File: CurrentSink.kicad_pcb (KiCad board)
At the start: 2 copper layers, 22 parts, among them J101 Test-Source, J102 Power-Jumper, J103 Power-Connector, Q301 STP55NF06L, U201 MCP6002, U401 TPS7A2401

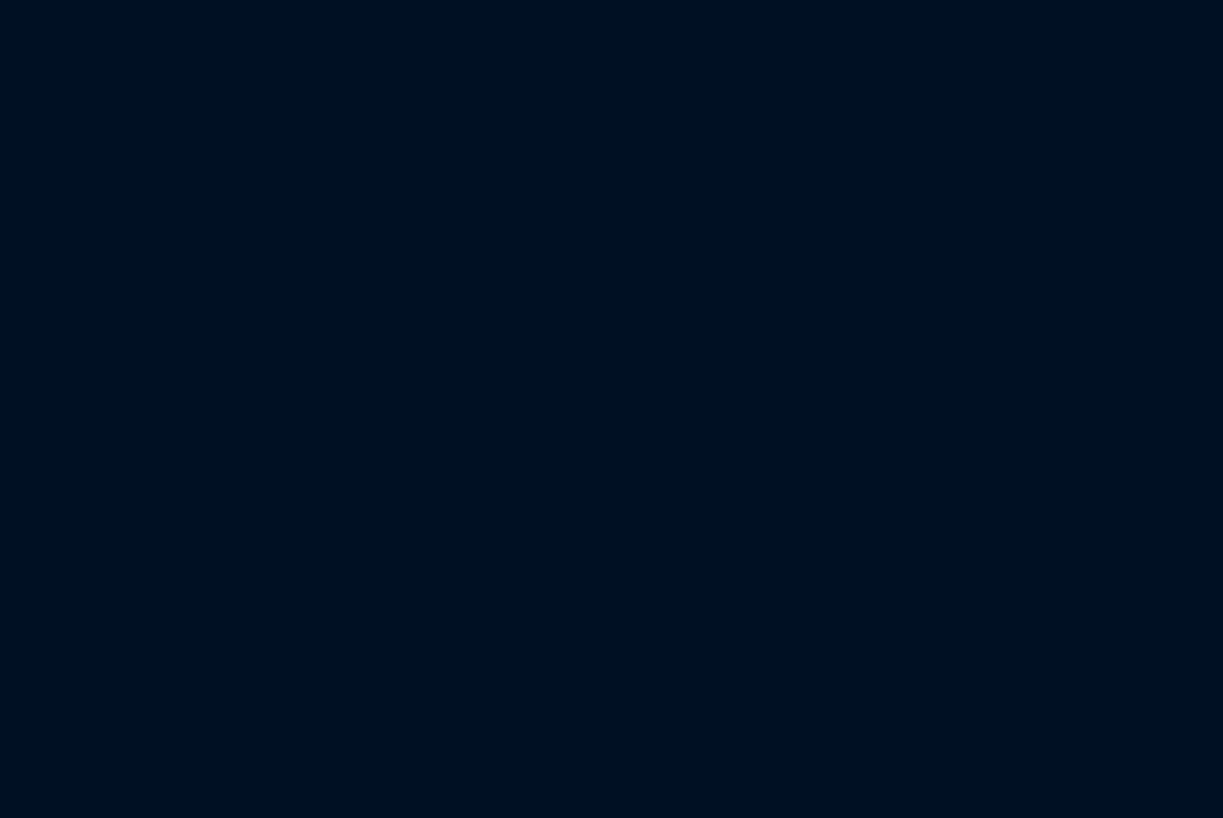
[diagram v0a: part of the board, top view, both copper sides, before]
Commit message: Added heatsink to schematic and PCB
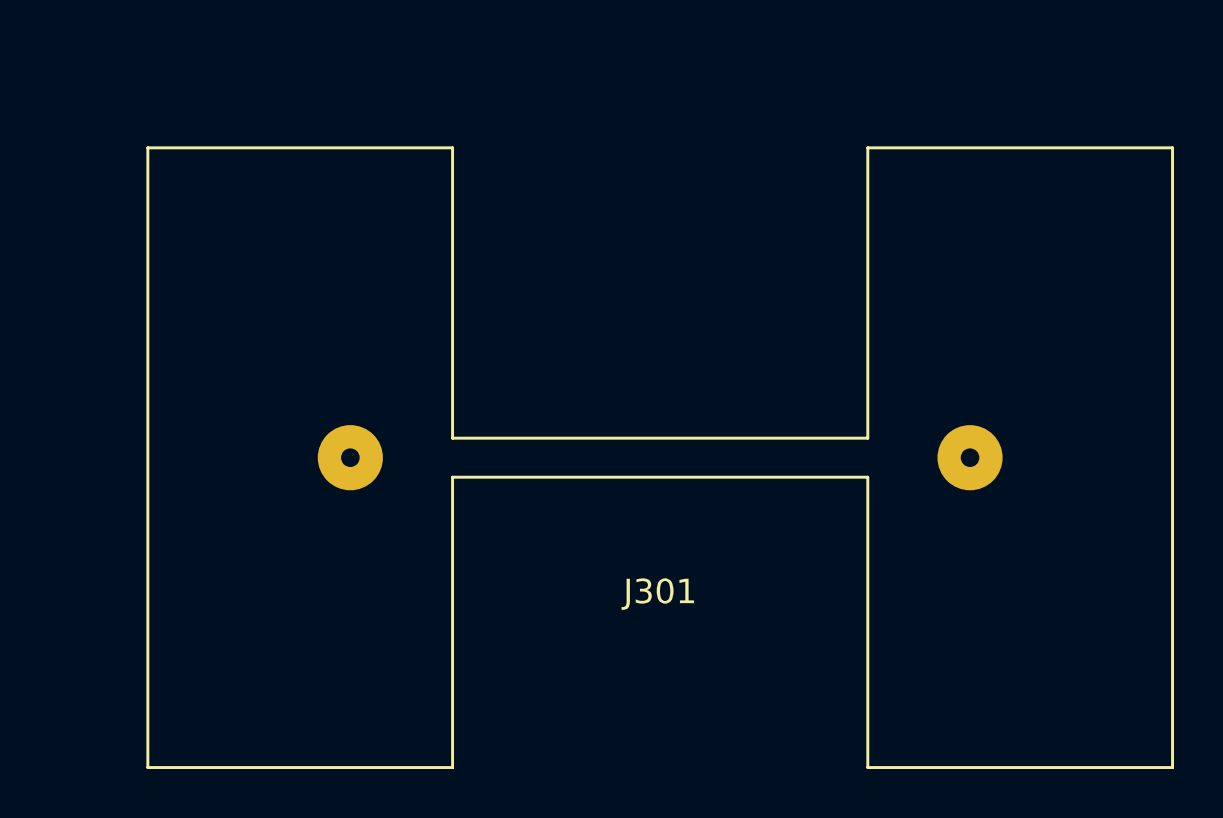
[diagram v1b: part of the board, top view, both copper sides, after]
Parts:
- added J301: Heatsink, f:Heatsink, F.Cu at (160.6, 81.0)

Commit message: Initial PCB component Placement
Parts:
- J101: value Test-Source -> Test; footprint Connector_PinHeader_1.27mm:PinHeader_1x02_P1.27mm_Vertical -> Connector_PinHeader_1.27mm:PinHeader_1x02_P1.27mm_Horizontal
- J103: value Power-Connector -> Ext. Pwr; footprint Connector_BarrelJack:BarrelJack_CUI_PJ-036AH-SMT_Horizontal -> TerminalBlock_Phoenix:TerminalBlock_Phoenix_PT-1,5-2-5.0-H_1x02_P5.00mm_Horizontal
- moved RV301 94.0 mm to (139.1, 146.4), turned to 270 degrees
- moved J103 85.2 mm to (118.0, 142.0)
- moved R301 84.9 mm to (142.9, 142.3), turned to 270 degrees
- moved J101 84.1 mm to (113.3, 141.5), turned to 270 degrees
- moved J102 75.8 mm to (107.2, 127.2)
- moved D201 74.9 mm to (140.6, 135.1)
- moved R302 74.4 mm to (143.2, 131.8), turned to 180 degrees
- moved RV201 73.7 mm to (129.6, 146.4), turned to 270 degrees
- moved R201 69.5 mm to (133.4, 142.3), turned to 270 degrees
- moved U201 65.0 mm to (137.2, 129.9), turned to 180 degrees
- moved R303 64.9 mm to (128.3, 123.0), turned to 270 degrees
- moved Q301 64.0 mm to (122.5, 117.0)
- moved R402 58.4 mm to (117.7, 133.0), turned to 270 degrees
- moved C404 57.7 mm to (129.1, 132.3), turned to 270 degrees
- moved R403 53.9 mm to (111.5, 133.0), turned to 90 degrees
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
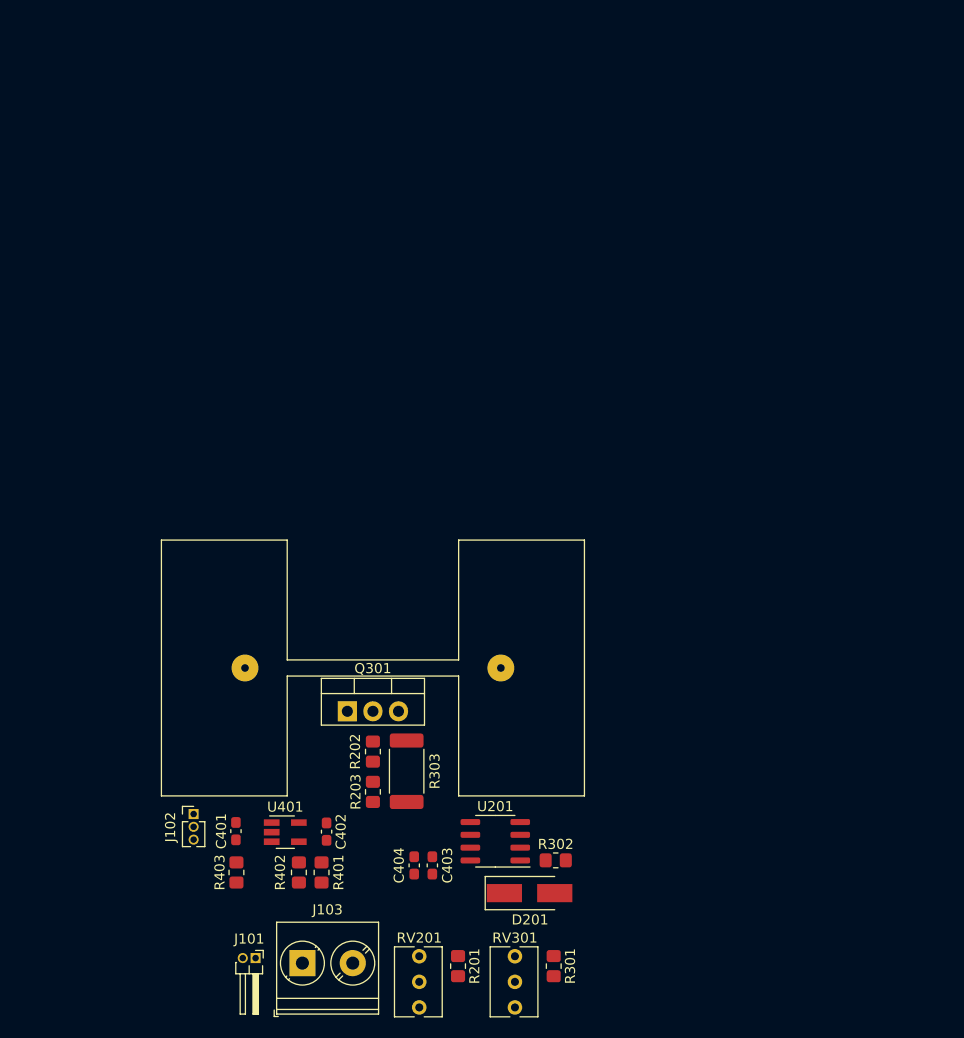
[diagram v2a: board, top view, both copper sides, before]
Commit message: PCB completed with Op-Amp mounted horizontally
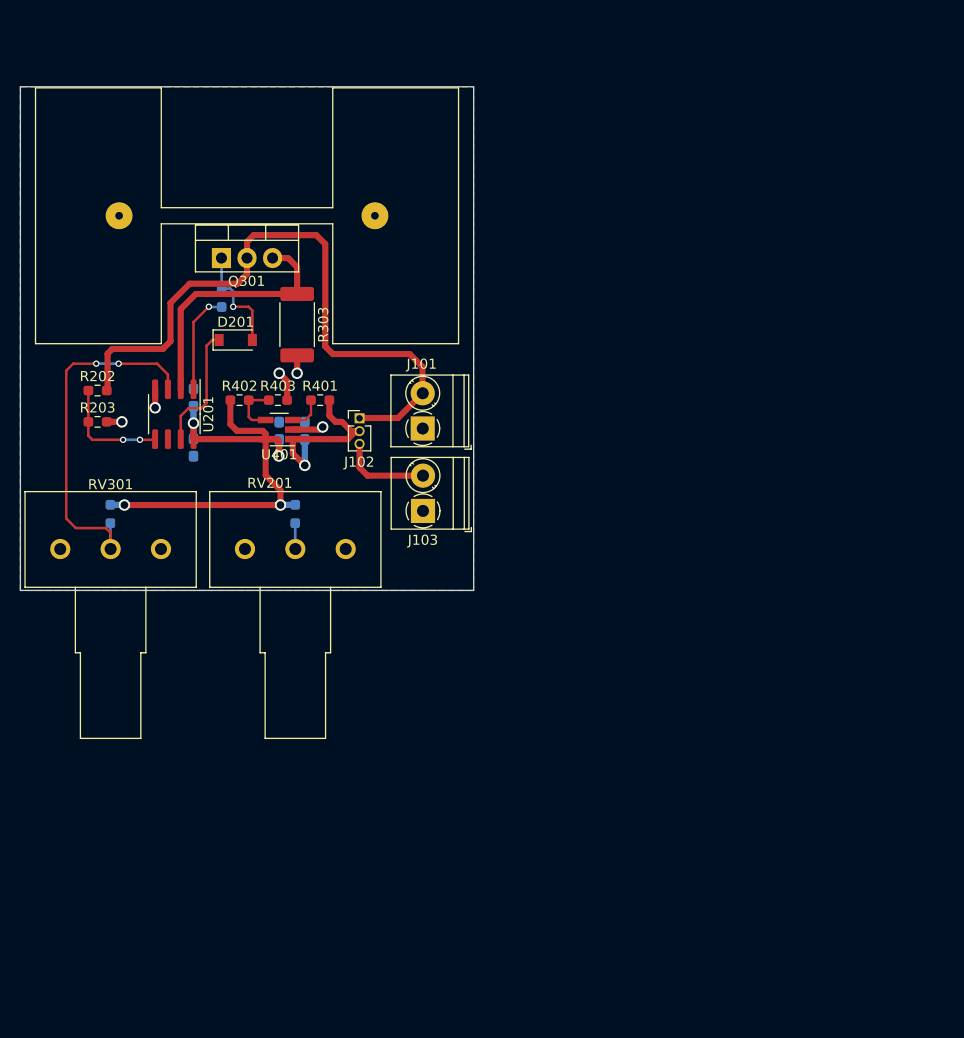
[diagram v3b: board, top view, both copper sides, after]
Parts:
- removed J301: Heatsink, f:Heatsink
- added H301: Heatsink, f:Heatsink, F.Cu at (112.5, 67.8)
- C401, C402, C403, C404: moved to B.Cu
- D201: value D -> 1N4148; footprint Diode_SMD:D_SMA_Handsoldering -> Diode_SMD:D_SOD-123
- J101: value Test -> Tst; footprint Connector_PinHeader_1.27mm:PinHeader_1x02_P1.27mm_Horizontal -> TerminalBlock_Phoenix:TerminalBlock_Phoenix_PT-1,5-2-3.5-H_1x02_P3.50mm_Horizontal
- J102: value Power-Jumper -> pwrJmp
- J103: value Ext. Pwr -> Pwr; footprint TerminalBlock_Phoenix:TerminalBlock_Phoenix_PT-1,5-2-5.0-H_1x02_P5.00mm_Horizontal -> TerminalBlock_Phoenix:TerminalBlock_Phoenix_PT-1,5-2-3.5-H_1x02_P3.50mm_Horizontal
- R201: value R -> 1K; footprint Resistor_SMD:R_0805_2012Metric_Pad1.20x1.40mm_HandSolder -> Resistor_SMD:R_0603_1608Metric_Pad0.98x0.95mm_HandSolder; moved to B.Cu
- R202, R203, R402: footprint Resistor_SMD:R_0805_2012Metric_Pad1.20x1.40mm_HandSolder -> Resistor_SMD:R_0603_1608Metric_Pad0.98x0.95mm_HandSolder
- R301: value R -> 6.2K; footprint Resistor_SMD:R_0805_2012Metric_Pad1.20x1.40mm_HandSolder -> Resistor_SMD:R_0603_1608Metric_Pad0.98x0.95mm_HandSolder; moved to B.Cu
- R302: footprint Resistor_SMD:R_0805_2012Metric_Pad1.20x1.40mm_HandSolder -> Resistor_SMD:R_0603_1608Metric_Pad0.98x0.95mm_HandSolder; moved to B.Cu
- R401: value 10K -> 0; footprint Resistor_SMD:R_0805_2012Metric_Pad1.20x1.40mm_HandSolder -> Resistor_SMD:R_0603_1608Metric_Pad0.98x0.95mm_HandSolder
- R403: value 0 -> 10K; footprint Resistor_SMD:R_0805_2012Metric_Pad1.20x1.40mm_HandSolder -> Resistor_SMD:R_0603_1608Metric_Pad0.98x0.95mm_HandSolder
- RV201, RV301: value R_POT -> 10K; footprint Potentiometer_THT:Potentiometer_Bourns_3266Y_Vertical -> f:POT_TTElect_P160KN
- moved R302 65.0 mm to (110.0, 75.9), turned to 270 degrees
- moved R301 62.9 mm to (98.9, 97.4)
- moved D201 62.2 mm to (111.4, 80.1)
- moved RV301 60.7 mm to (99.0, 100.9), turned to 0 degrees
- moved J101 55.1 mm to (129.9, 88.9), turned to 90 degrees
- moved U201 53.0 mm to (105.3, 87.5), turned to 270 degrees
- moved C403 47.8 mm to (107.2, 90.8)
- moved R201 47.7 mm to (117.3, 97.4)
- moved R402 47.3 mm to (111.8, 86.1), turned to 0 degrees
- moved RV201 47.1 mm to (117.3, 100.9), turned to 0 degrees
- moved R403 47.1 mm to (115.6, 86.1), turned to 0 degrees
- moved R401 46.9 mm to (119.8, 86.1), turned to 0 degrees
- moved Q301 46.7 mm to (110.0, 72.0)
- moved J103 46.5 mm to (130.0, 97.1), turned to 90 degrees
- moved R203 45.8 mm to (97.7, 88.3), turned to 0 degrees
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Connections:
- net /V-ctrl renamed /Vctrl
- net /V-pos-tst renamed /tstV+
- C401 pad 1: /V-pos-src -> /regIN
- C402 pad 1: /2.5V-reg -> /2.5V
- C403 pad 1: /2.5V-reg -> /2.5V
- C404 pad 1: /2.5V-reg -> /2.5V
- J102 pad 2: /V-pos-src -> /regIN
- J102 pad 3: /V-pos-src -> /pwrV+
- J103 pad 1: /V-pos-src -> GND
- J103 pad 2: GND -> /pwrV+
- R201 pad 1: Net-(R201-Pad1) -> /2.5V
- R201 pad 2: GND -> Net-(R201-Pad2)
- R301 pad 1: Net-(R301-Pad1) -> /2.5V
- R301 pad 2: GND -> Net-(R301-Pad2)
- R401 pad 1: /2.5V-reg -> /Power-Reg/regEN
- R401 pad 2: /Power-Reg/FB -> /regIN
- R402 pad 1: /Power-Reg/FB -> /2.5V
- R402 pad 2: GND -> /Power-Reg/regFB
- R403 pad 1: Net-(R403-Pad1) -> /Power-Reg/regFB
- R403 pad 2: /V-pos-src -> GND
- RV201 pad 1: Net-(RV201-Pad1) -> GND
- RV201 pad 2: /2.5V-reg -> Net-(R201-Pad2)
- RV201 pad 3: Net-(R201-Pad1) -> Net-(RV201-Pad3)
- RV301 pad 1: Net-(RV301-Pad1) -> GND
- RV301 pad 2: /2.5V-reg -> Net-(R301-Pad2)
- RV301 pad 3: Net-(R301-Pad1) -> Net-(RV301-Pad3)
- U201 pad 3: Net-(R301-Pad1) -> Net-(R301-Pad2)
- U201 pad 5: Net-(R201-Pad1) -> Net-(R202-Pad2)
- U201 pad 6: Net-(R202-Pad2) -> Net-(R201-Pad2)
- U201 pad 8: /2.5V-reg -> /2.5V
- U401 pad 1: /V-pos-src -> /regIN
- U401 pad 3: Net-(R403-Pad1) -> /Power-Reg/regEN
- U401 pad 4: /Power-Reg/FB -> /Power-Reg/regFB
- U401 pad 5: /2.5V-reg -> /2.5V
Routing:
- net /tstV+: track 0.00 -> 65.3 mm
- net /2.5V: track 0.00 -> 48.8 mm, vias 0 -> 4
- net Net-(R301-Pad2): track 0.00 -> 36.2 mm, vias 0 -> 2
- net Net-(Q301-Pad3): track 0.00 -> 25.6 mm
- net /regIN: track 0.00 -> 17.9 mm, vias 0 -> 1
- net Net-(D201-Pad1): track 0.00 -> 12.6 mm
- net Net-(R202-Pad2): track 0.00 -> 11.4 mm, vias 0 -> 2
- net GND: track 0.00 -> 11.1 mm, vias 0 -> 5
- net /Vctrl: track 0.00 -> 10.9 mm, vias 0 -> 1
- net Net-(R302-Pad2): track 0.00 -> 10.1 mm, vias 0 -> 1
- net /pwrV+: track 0.00 -> 8.99 mm
- net /Power-Reg/regFB: track 0.00 -> 5.46 mm
- net /Power-Reg/regEN: track 0.00 -> 3.45 mm
- net Net-(R201-Pad2): track 0.00 -> 2.58 mm
- added copper zone on B.Cu, net GND
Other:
- board outline added: 45 x 50 mm
- net class Default: clearance 0.2 -> 0.2032; trace_width 0.25 -> 0.254; via_dia 0.8 -> 0.635; via_drill 0.4 -> 0.381
- net class Power added: clearance 0.3048, trace_width 0.6096, via_dia 1.143, via_drill 0.762
- rule trace_clearance: 0.2 -> 0.2032
- rule trace_min: 0.2 -> 0.2032
- rule via_min_size: 0.4 -> 0.4064

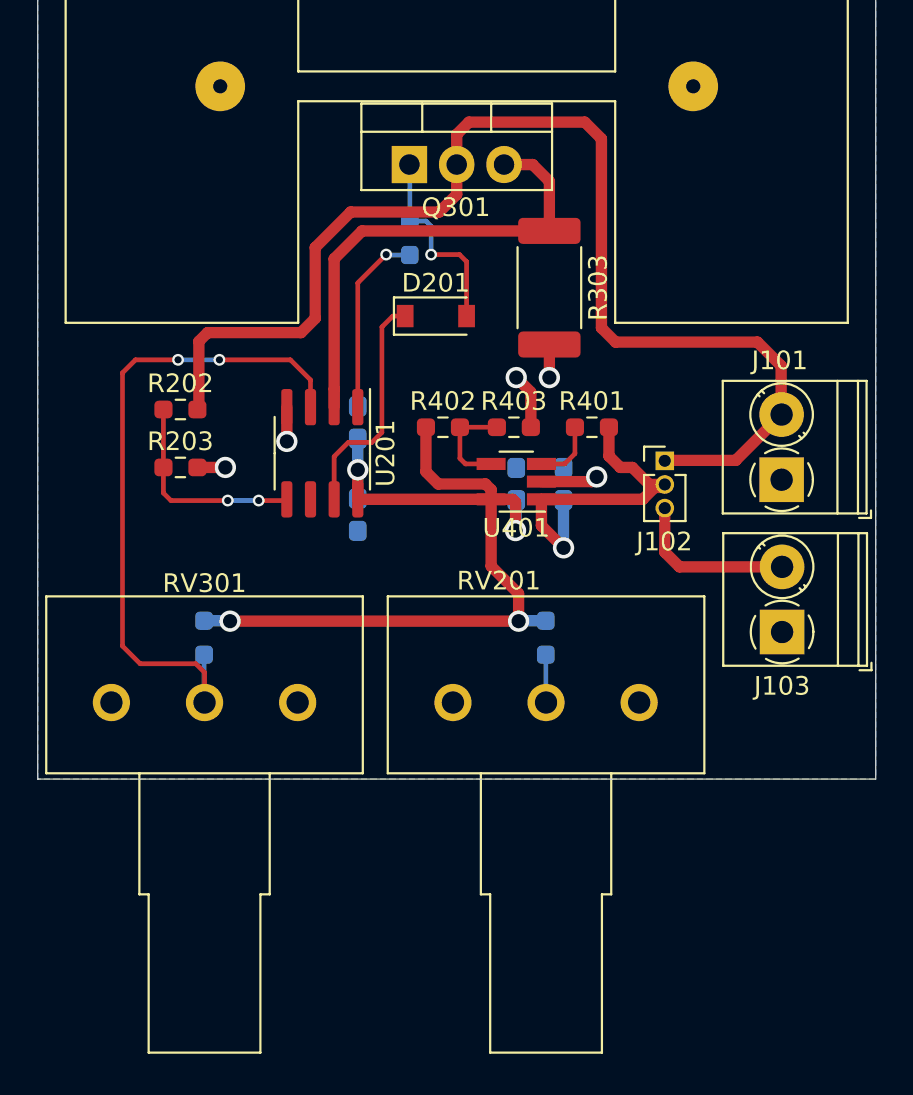
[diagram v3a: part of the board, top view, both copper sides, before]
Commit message: Changed the Op-Amp to be vertical and switched the power input side
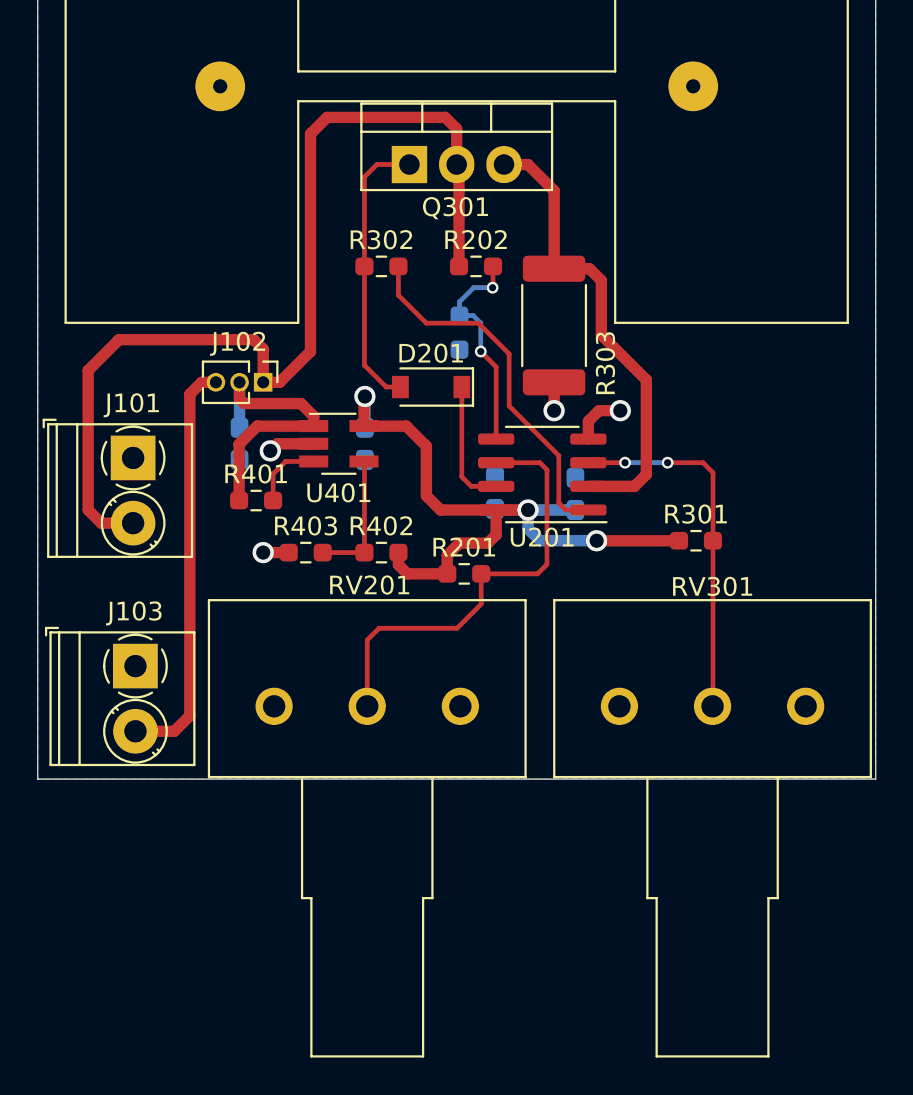
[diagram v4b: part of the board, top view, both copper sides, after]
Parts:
- R201, R301, R302: moved to F.Cu
- R203: moved to B.Cu
- moved J101 34.8 mm to (95.1, 87.8), turned to 270 degrees
- moved J103 34.8 mm to (95.2, 98.9), turned to 270 degrees
- moved RV301 27.3 mm to (126.2, 101.1)
- moved R301 26.9 mm to (125.3, 92.2), turned to 0 degrees
- moved J102 22.0 mm to (102.1, 83.7), turned to 270 degrees
- moved R401 18.5 mm to (101.7, 90.0), turned to 180 degrees
- moved R202 17.6 mm to (113.5, 77.5), turned to 0 degrees
- moved C401 17.5 mm to (100.8, 87.0), turned to 270 degrees
- moved R203 16.6 mm to (112.6, 81.0), turned to 270 degrees
- moved R403 13.0 mm to (104.4, 92.8), turned to 180 degrees
- moved C402 12.3 mm to (118.9, 89.7)
- moved U201 11.9 mm to (117.1, 88.6), turned to 180 degrees
- moved U401 9.74 mm to (106.2, 87.0), turned to 0 degrees
- moved RV201 9.60 mm to (107.7, 101.1)
- moved C404 8.41 mm to (107.6, 87.0), turned to 270 degrees
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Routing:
- net Net-(R201-Pad2): track 2.58 -> 23.8 mm
- net Net-(R301-Pad2): track 36.2 -> 19.5 mm
- net /pwrV+: track 8.99 -> 22.2 mm
- net /tstV+: track 65.3 -> 53.1 mm
- net /2.5V: track 48.8 -> 38.1 mm, vias 4 -> 3
- net Net-(R302-Pad2): track 10.1 -> 19.6 mm, vias 1 -> 0
- net Net-(D201-Pad1): track 12.6 -> 6.88 mm
- net /Vctrl: track 10.9 -> 15.2 mm, vias 1 -> 0
- net GND: track 11.1 -> 8.29 mm, vias 5 -> 4
- net /regIN: track 17.9 -> 16.0 mm, vias 1 -> 0
- net /Power-Reg/regFB: track 5.46 -> 7.14 mm
- net Net-(R202-Pad2): track 11.4 -> 12.1 mm
- net Net-(Q301-Pad3): track 25.6 -> 25.1 mm
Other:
- net class Power: clearance 0.3048 -> 0.1524
